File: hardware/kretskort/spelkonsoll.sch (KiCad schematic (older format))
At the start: 35 parts, among them J1 USB_C_Receptacle_USB2.0, SW1 SW_Push, SW10 SW_Push, SW11 SW_Push, SW12 SW_Push, SW2 SW_Push, SW3 SW_Push, SW4 SW_Push, SW5 SW_Push, SW6 SW_Push, SW7 SW_Push, SW8 SW_Push, SW9 SW_Push, U1 BQ24202DGN, U2 ESP32-DEVKITC-32D, U3 ILI9488

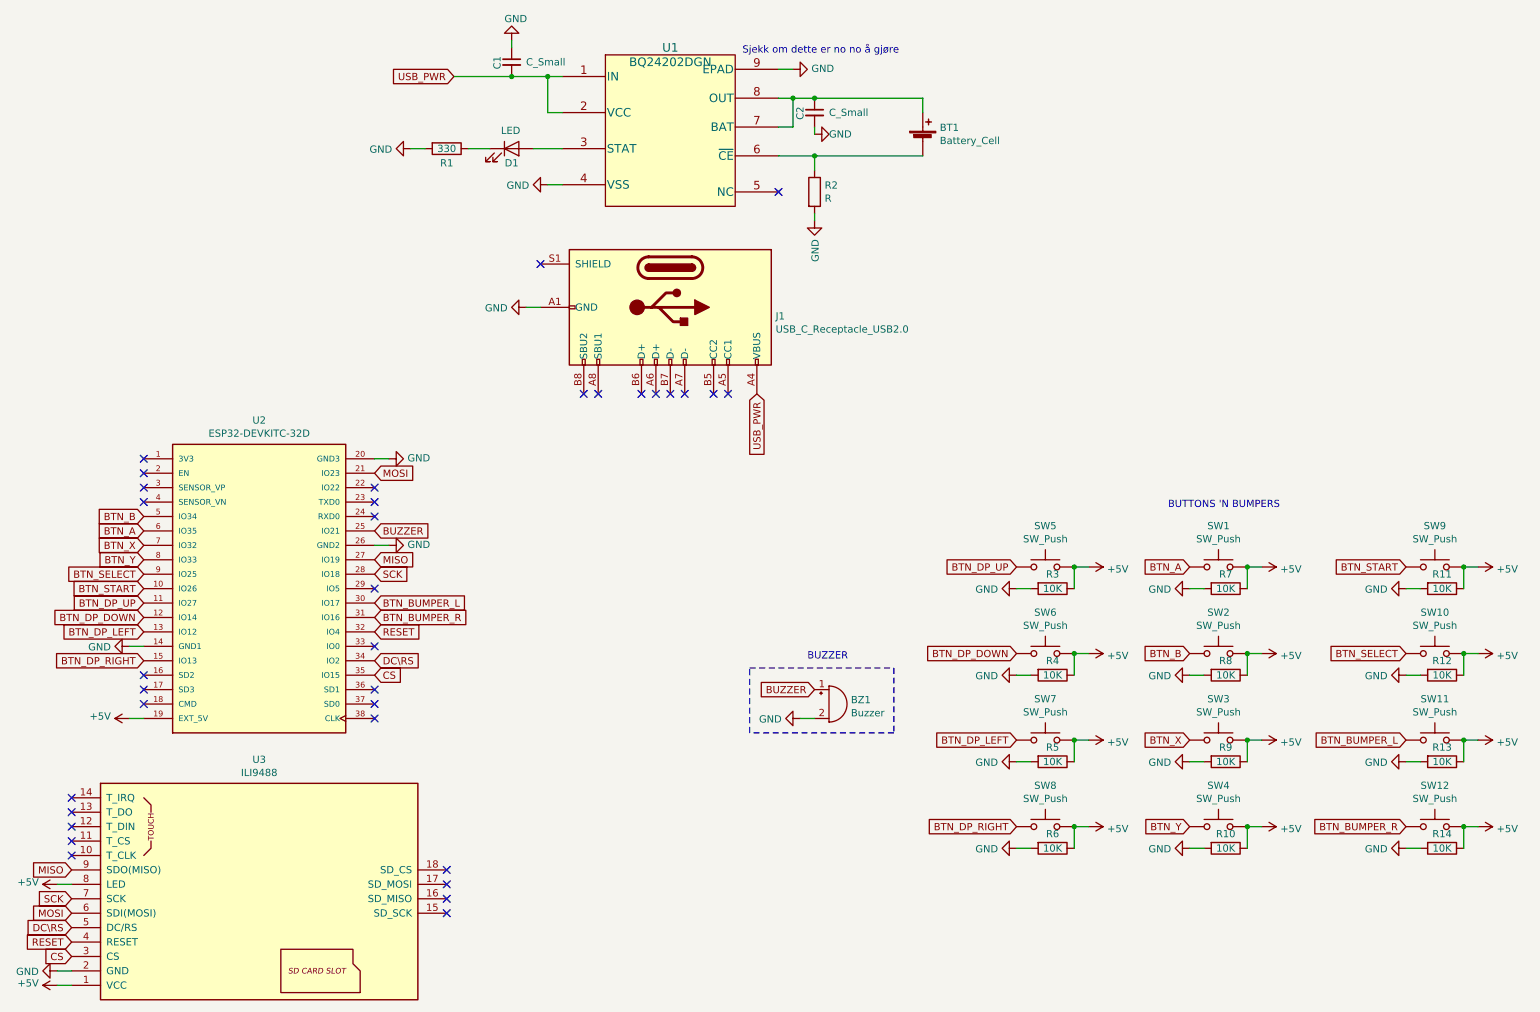
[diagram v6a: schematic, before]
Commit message: started on v0.2 moved resistors and added silkscreen for inputs on the ESP32
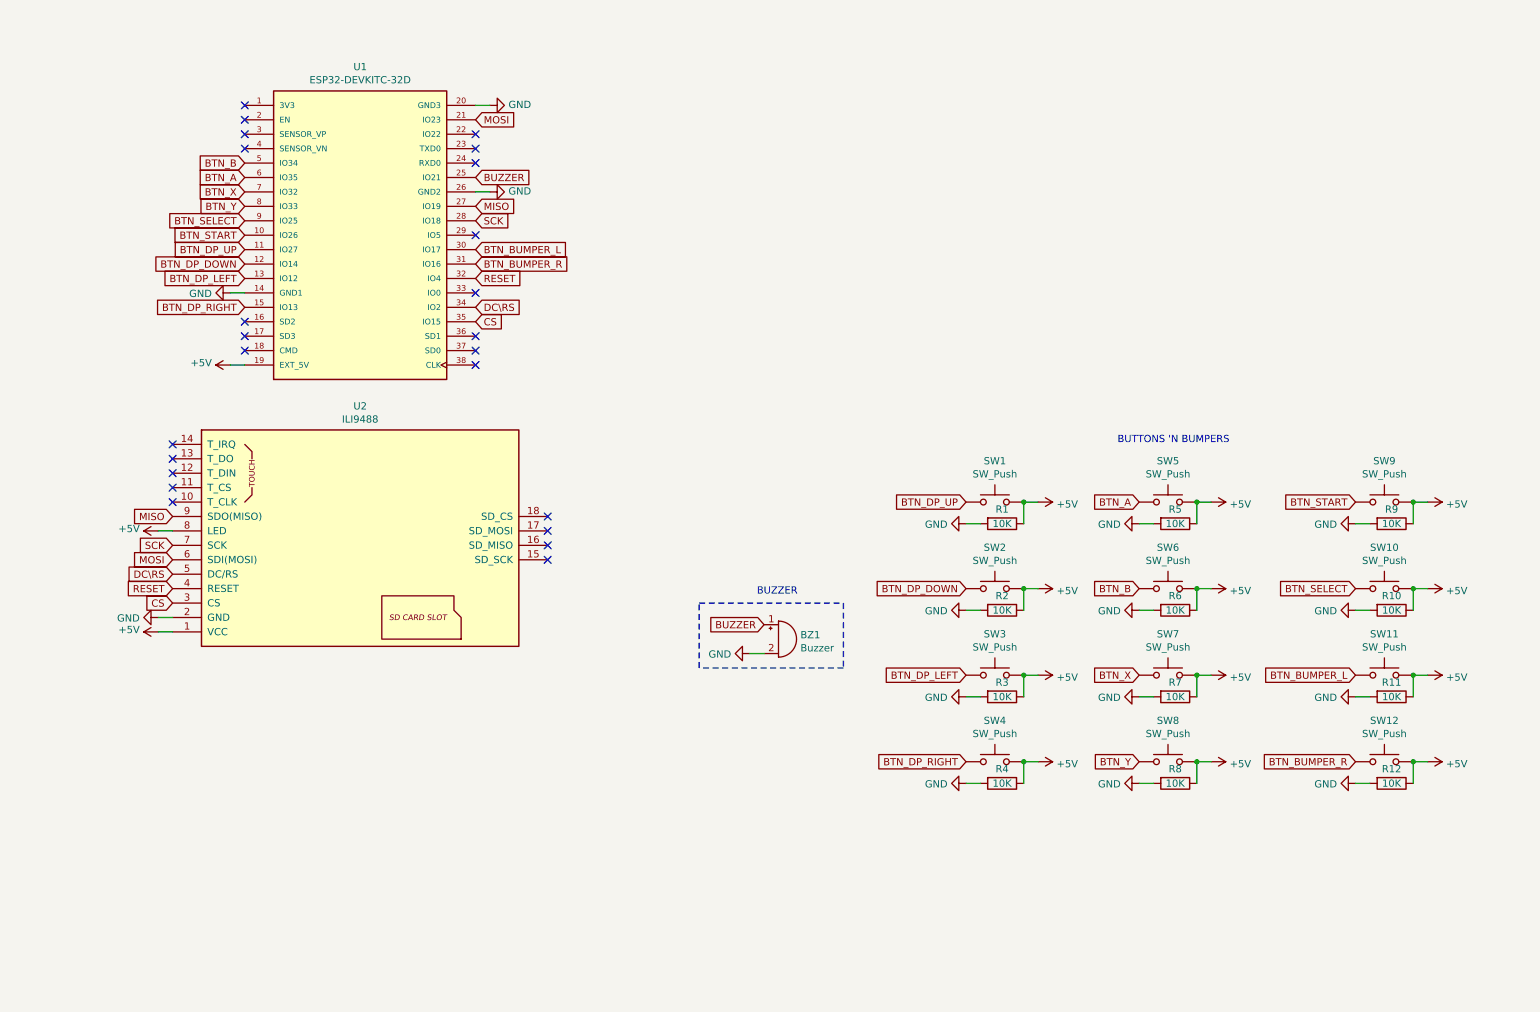
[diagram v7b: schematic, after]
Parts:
- removed BT1: Battery_Cell, footprints:18650holder, symbol Device:Battery_Cell
- removed C1, C2: C_Small, symbol Device:C_Small
- removed D1: LED, symbol Device:LED
- removed J1: USB_C_Receptacle_USB2.0, symbol Connector:USB_C_Receptacle_USB2.0
- removed R1: 330, symbol Device:R
- removed R2: R, symbol Device:R
- removed U1: BQ24202DGN, symbol Strøm:BQ24202DGN
- renumbered R3 to R1, R12 to R10, R13 to R11, R14 to R12, R4 to R2, R5 to R3, R6 to R4, R7 to R5, R8 to R6, R9 to R7, R10 to R8, R11 to R9, SW5 to SW1, SW6 to SW2, SW7 to SW3, SW8 to SW4, SW1 to SW5, SW2 to SW6, SW3 to SW7, SW4 to SW8, U2 to U1, U3 to U2
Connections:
- no-connect marks 34 -> 24
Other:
- note removed: "Sjekk om dette er no no å gjøre"
- moved on the sheet: BZ1, R1, R10, R11, R12, R2, R3, R4, R5, R6, R7, R8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

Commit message: Added schema from v0.1, deleted buttons
Moved resistors and deleted start, select, and shoulder buttons
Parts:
- removed BZ1: Buzzer, Buzzer_Beeper:Buzzer_15x7.5RM7.6, symbol Device:Buzzer
- removed R10, R11, R12, R9: 10K, Resistor_THT:R_Axial_DIN0207_L6.3mm_D2.5mm_P7.62mm_Horizontal, symbol Device:R
- removed SW10, SW9: SW_Push, footprints:B3F1052, symbol Switch:SW_Push
- removed SW11, SW12: SW_Push, footprints:B3F-3152, symbol Switch:SW_Push
- R1, R2, R3, R4, R5, R6, R7, R8: symbol Device:R -> spelkonsoll-rescue:R-Device
- SW1, SW2, SW3, SW4, SW5, SW6, SW7, SW8: symbol Switch:SW_Push -> spelkonsoll-rescue:SW_Push-Switch
- U1: symbol ESP32-DEVKITC-32D:ESP32-DEVKITC-32D -> spelkonsoll-rescue:ESP32-DEVKITC-32D-ESP32-DEVKITC-32D
- U2: symbol ILI9488:ILI9488 -> spelkonsoll-rescue:ILI9488-ILI9488
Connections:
- net BTN_BUMPER_L is gone; now on net DC\RS: U1.30 (IO17)
- net BTN_BUMPER_R is gone; now on net CS: U1.31 (IO16)
- net BTN_SELECT is gone; now on net BTN_Y: U1.9 (IO25)
- net BTN_START is gone; now on net BTN_DP_UP: U1.10 (IO26)
- net BUZZER is gone; now on net BTN_A: U1.25 (IO21)
- net BTN_A: no longer U1.6 (IO35)
- net BTN_B: now also U1.7 (IO32); no longer U1.5 (IO34)
- net BTN_DP_DOWN: now also U1.11 (IO27); no longer U1.12 (IO14)
- net BTN_DP_LEFT: now also U1.12 (IO14); no longer U1.13 (IO12)
- net BTN_DP_UP: no longer U1.11 (IO27)
- net BTN_X: now also U1.8 (IO33); no longer U1.7 (IO32)
- net BTN_Y: no longer U1.8 (IO33)
- net CS: no longer U1.35 (IO15)
- net DC\RS: no longer U1.34 (IO2)
- no-connect marks 24 -> 29
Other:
- note added: "BUTTONS ’N"
- note removed: "BUTTONS 'N BUMPERS"
- note removed: "BUZZER"
- moved on the sheet: R1, R2, R3, R4, R5, R6, R7, R8, SW1, SW2, SW3, SW4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
